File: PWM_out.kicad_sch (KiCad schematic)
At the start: 32 parts, among them J11 Conn_01x03_Pin, J12 Conn_01x03_Pin, J13 Conn_01x03_Pin, J14 Conn_01x03_Pin, J2 Conn_01x03_Pin, J3 Conn_01x03_Pin, J4 Conn_01x03_Pin, J5 Conn_01x03_Pin

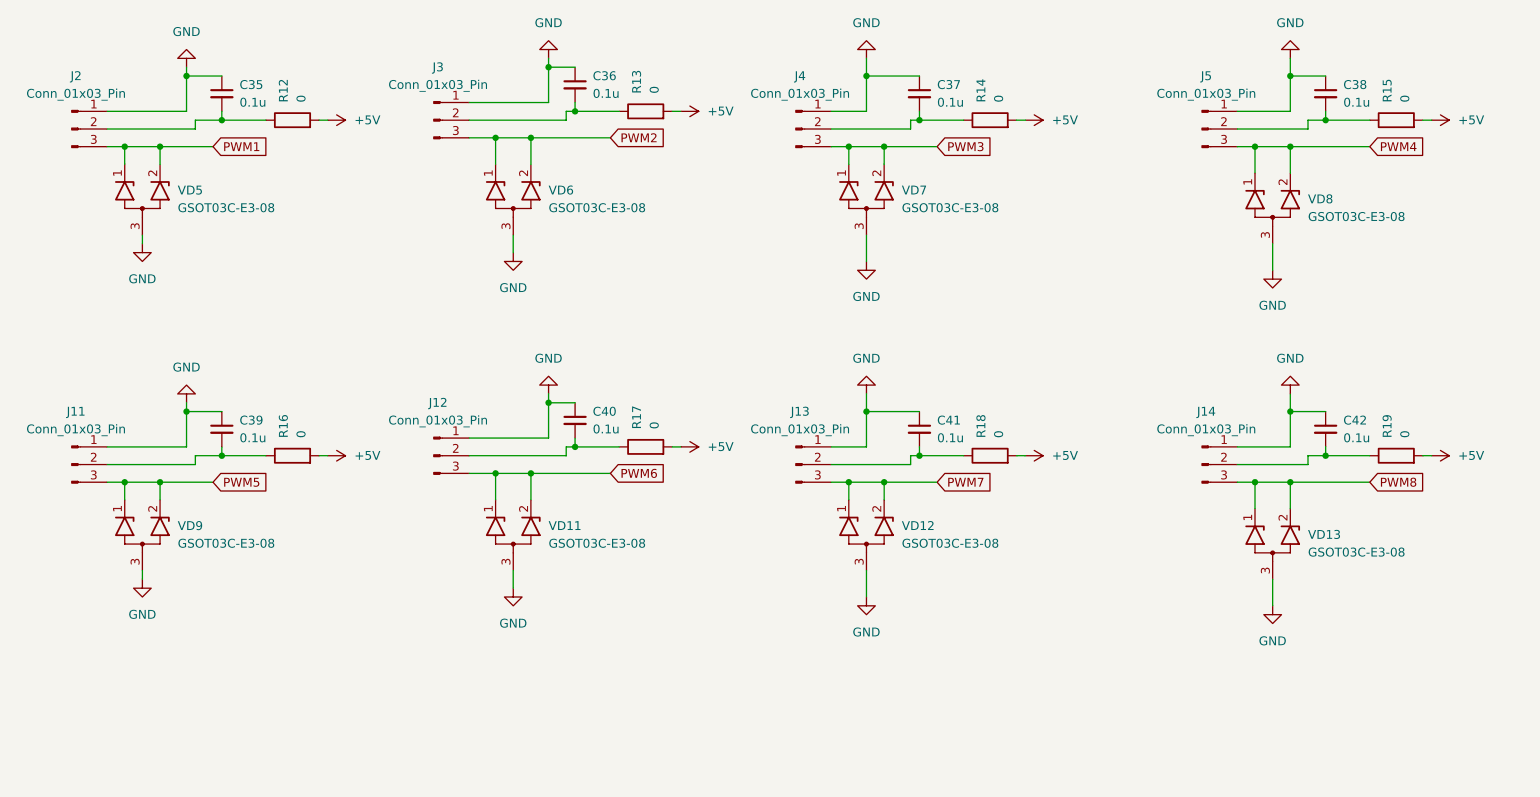
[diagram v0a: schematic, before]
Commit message: feat: доработана схема питания, расчечены габариты печатной платы
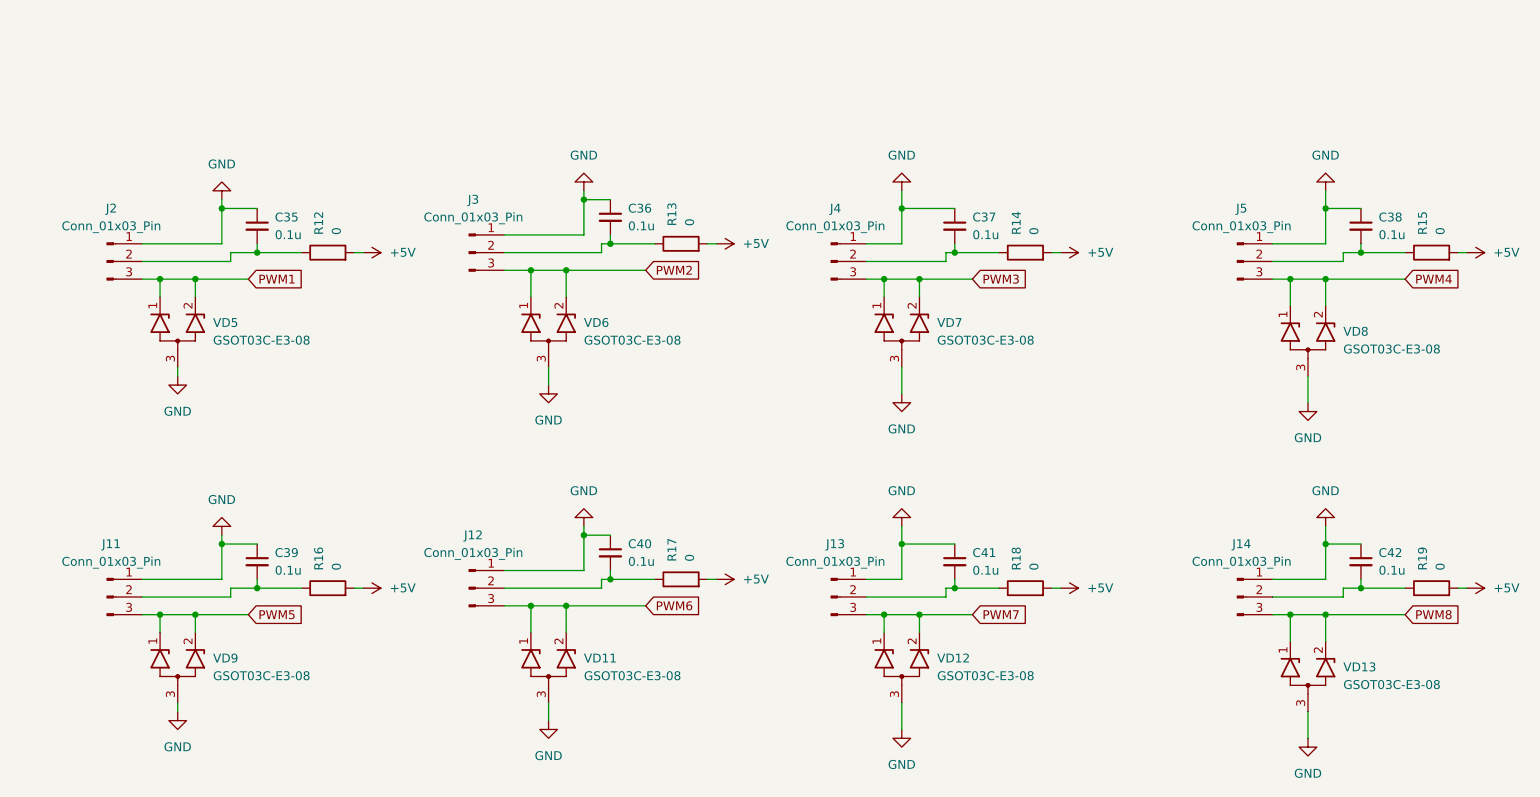
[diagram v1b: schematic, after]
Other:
- moved on the sheet: C35, C36, C37, C38, C39, C40, C41, C42, J11, J12, J13, J14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

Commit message: feat: добавлены светодиоды, размещены почти все компоненты кроме модулей IMU
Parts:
- VD11, VD12, VD13, VD5, VD6, VD7, VD8, VD9: footprint Package_TO_SOT_SMD:SOT-23_Handsoldering -> Package_TO_SOT_SMD:SOT-23
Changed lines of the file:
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@@
 			)
 		)
-		(property "Footprint" "Package_TO_SOT_SMD:SOT-23_Handsoldering"
+		(property "Footprint" "Package_TO_SOT_SMD:SOT-23"
 			(at 116.84 121.92 0)
 			(hide yes)
@@
 			)
 		)
-		(property "Footprint" "Package_TO_SOT_SMD:SOT-23_Handsoldering"
+		(property "Footprint" "Package_TO_SOT_SMD:SOT-23"
 			(at 226.06 74.93 0)
 			(hide yes)
@@
 			)
 		)
-		(property "Footprint" "Package_TO_SOT_SMD:SOT-23_Handsoldering"
+		(property "Footprint" "Package_TO_SOT_SMD:SOT-23"
 			(at 167.64 121.92 0)
 			(hide yes)
@@
 			)
 		)
-		(property "Footprint" "Package_TO_SOT_SMD:SOT-23_Handsoldering"
+		(property "Footprint" "Package_TO_SOT_SMD:SOT-23"
 			(at 116.84 73.66 0)
 			(hide yes)
@@
 			)
 		)
-		(property "Footprint" "Package_TO_SOT_SMD:SOT-23_Handsoldering"
+		(property "Footprint" "Package_TO_SOT_SMD:SOT-23"
 			(at 226.06 123.19 0)
 			(hide yes)
@@
 			)
 		)
-		(property "Footprint" "Package_TO_SOT_SMD:SOT-23_Handsoldering"
+		(property "Footprint" "Package_TO_SOT_SMD:SOT-23"
 			(at 63.5 121.92 0)
 			(hide yes)
@@
 			)
 		)
-		(property "Footprint" "Package_TO_SOT_SMD:SOT-23_Handsoldering"
+		(property "Footprint" "Package_TO_SOT_SMD:SOT-23"
 			(at 167.64 73.66 0)
 			(hide yes)
@@
 			)
 		)
-		(property "Footprint" "Package_TO_SOT_SMD:SOT-23_Handsoldering"
+		(property "Footprint" "Package_TO_SOT_SMD:SOT-23"
 			(at 63.5 73.66 0)
 			(hide yes)
